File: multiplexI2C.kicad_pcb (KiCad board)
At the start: 2 copper layers, 48.3 x 71.1 mm, 60 parts, among them J1 Screw_Terminal_01x04, J17 Conn_01x04_Pin, J18 PinSocket_1x20_P2.54mm_Vertic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, J19 PinSocket_1x20_P2.54mm_Vertic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, J2 Screw_Terminal_01x04, J20 Screw_Terminal_01x02, J3 Screw_Terminal_01x04, J4 Screw_Terminal_01x04, J5 Screw_Terminal_01x04, J6 Screw_Terminal_01x04, J7 Screw_Terminal_01x04, J8 Screw_Terminal_01x04, J9 header_0.25sqmm_1x04_P4.2mm_D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, U1 TCA9548A, U2 RFM95W-915S2

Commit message: cleaning up details forbetter BOM generator.
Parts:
- J9: value header_0.25sqmm_1x04_P4.2mm_D0.65mm_OD1.7mm -> PinSocket__1x04_P2.54mm_Vertical
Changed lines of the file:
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@@
 		(sheetname "Root")
 		(sheetfile "multiplexI2C.kicad_sch")
-		(attr exclude_from_pos_files)
+		(attr exclude_from_pos_files exclude_from_bom)
 		(fp_circle
 			(center 0 0)
@@
 			)
 		)
-		(property "Description" "Generic screw terminal, single row, 01x04, script generated (kicad-library-utils/schlib/autogen/connector/)"
+		(property "Description" "Generic screw terminal, single row, 01x04"
 			(at 0 0 180)
 			(unlocked yes)
@@
 			)
 		)
-		(property "Description" "Generic screw terminal, single row, 01x04, script generated (kicad-library-utils/schlib/autogen/connector/)"
+		(property "Description" "Generic screw terminal, single row, 01x04"
 			(at 0 0 180)
 			(unlocked yes)
@@
 			)
 		)
-		(property "Description" "Generic screw terminal, single row, 01x04, script generated (kicad-library-utils/schlib/autogen/connector/)"
+		(property "Description" "Generic screw terminal, single row, 01x04"
 			(at 0 0 180)
 			(unlocked yes)
@@
 		(layer "F.Cu")
 		(at 89.916 64.77)
-		(descr "sockets for blackpill stm32f401")
+		(descr "take-off from blackpill stm32f401")
 		(tags "blackpill bluepill pinSockets")
 		(property "Reference" "J**2"
@@
 			)
 		)
-		(property "Description" "extra pads for one side of blackpill (stm32f401) pins 21-40"
+		(property "Description" "unpopulated connections"
 			(at 0 0 0)
 			(unlocked yes)
@@
 		(sheetname "Root")
 		(sheetfile "multiplexI2C.kicad_sch")
-		(attr through_hole)
+		(attr through_hole exclude_from_bom)
 		(fp_line
 			(start -2.286 -25.146)
@@
 			)
 		)
-		(property "Description" "one side of blackpill (stm32f401) pins 21-40"
+		(property "Description" "20P header (for blackpill)"
 			(at 0 0 0)
 			(unlocked yes)
@@
 			)
 		)
-		(property "Description" "Generic screw terminal, single row, 01x04, script generated (kicad-library-utils/schlib/autogen/connector/)"
+		(property "Description" "Generic screw terminal, single row, 01x04"
 			(at 0 0 180)
 			(unlocked yes)
@@
 		(sheetname "Root")
 		(sheetfile "multiplexI2C.kicad_sch")
-		(attr exclude_from_pos_files)
+		(attr exclude_from_pos_files exclude_from_bom)
 		(fp_circle
 			(center 0 0)
@@
 			)
 		)
-		(property "Description" "Generic screw terminal, single row, 01x04, script generated (kicad-library-utils/schlib/autogen/connector/)"
+		(property "Description" "Generic screw terminal, single row, 01x04"
 			(at 0 0 180)
 			(unlocked yes)
@@
 		(sheetname "Root")
 		(sheetfile "multiplexI2C.kicad_sch")
-		(attr exclude_from_pos_files)
+		(attr exclude_from_pos_files exclude_from_bom)
 		(fp_circle
 			(center 0 0)
@@
 			)
 		)
-		(property "Description" "Generic connector, single row, 01x04, script generated"
+		(property "Description" "Generic connector, single row, 01x04"
 			(at 0 0 -90)
 			(unlocked yes)
@@
 			)
 		)
-		(property "Description" "Generic screw terminal, single row, 01x04, script generated (kicad-library-utils/schlib/autogen/connector/)"
+		(property "Description" "Generic screw terminal, single row, 01x04"
 			(at 0 0 180)
 			(unlocked yes)
@@
 		(layer "F.Cu")
 		(at 86.165 64.605)
-		(descr "sockets for blackpill stm32f401")
+		(descr "take-off  from blackpill stm32f401")
 		(tags "blackpill bluepill pinSockets")
 		(property "Reference" "J**1"
@@
 			)
 		)
-		(property "Description" "extra takeoff pads for one side of blackpill (stm32f401) pins 1-20"
+		(property "Description" "unpopulated connections"
 			(at 0 0 0)
 			(unlocked yes)
@@
 		(sheetname "Root")
 		(sheetfile "multiplexI2C.kicad_sch")
-		(attr through_hole)
+		(attr through_hole exclude_from_bom)
 		(fp_line
 			(start -6.096 -25.146)
@@
 			)
 		)
-		(property "Description" "one side of blackpill (stm32f401) pins 1-20"
+		(property "Description" "20P header (for blackpill)"
 			(at 0 0 0)
 			(unlocked yes)
@@
 			)
 		)
-		(property "Description" "Generic screw terminal, single row, 01x04, script generated (kicad-library-utils/schlib/autogen/connector/)"
+		(property "Description" "Generic screw terminal, single row, 01x04"
 			(at 0 0 180)
 			(unlocked yes)
@@
 		(layer "F.Cu")
 		(at 65.61 92.825 -90)
-		(descr "Through hole straight socket strip, 1x04, 2.54mm pitch, single row (from Kicad 4.0.7), script generated")
+		(descr "header for ssd1306")
 		(tags "Through hole socket strip THT 1x04 2.54mm single row")
 		(property "Reference" "J9"
@@
 			)
 		)
-		(property "Value" "header_0.25sqmm_1x04_P4.2mm_D0.65mm_OD1.7mm"
-			(at 6.705 3.55 180)
+		(property "Value" "PinSocket__1x04_P2.54mm_Vertical"
+			(at 23.655 3.43 -90)
 			(layer "F.Fab")
 			(effects
@@
 			)
 		)
-		(property "Description" "4P I2C header for SSD1306 module"
+		(property "Description" "4P header (I2C for SSD1306 module)"
 			(at 0 0 -90)
 			(unlocked yes)
@@
 			)
 		)
+		(property "Manufacturer" "JILN"
+			(at 0 0 -90)
+			(unlocked yes)
+			(layer "F.Fab")
+			(hide yes)
+			(effects
+				(font
+					(size 1 1)
+					(thickness 0.15)
+				)
+			)
+		)
+		(property "MfgPart" "228050104ANG1SYA01"
+			(at 0 0 -90)
+			(unlocked yes)
+			(layer "F.Fab")
+			(hide yes)
+			(effects
+				(font
+					(size 1 1)
+					(thickness 0.15)
+				)
+			)
+		)
+		(property "MountType" "PTH"
+			(at 0 0 -90)
+			(unlocked yes)
+			(layer "F.Fab")
+			(hide yes)
+			(effects
+				(font
+					(size 1 1)
+					(thickness 0.15)
+				)
+			)
+		)
+		(property "Notes" "or equivalent"
+			(at 0 0 -90)
+			(unlocked yes)
+			(layer "F.Fab")
+			(hide yes)
+			(effects
+				(font
+					(size 1 1)
+					(thickness 0.15)
+				)
+			)
+		)
 		(sheetname "Root")
 		(sheetfile "multiplexI2C.kicad_sch")
@@
 		(sheetname "Root")
 		(sheetfile "multiplexI2C.kicad_sch")
-		(attr exclude_from_pos_files)
+		(attr exclude_from_pos_files exclude_from_bom)
 		(fp_circle
 			(center 0 0)
@@
 			)
 		)
-		(property "Description" "Generic screw terminal, single row, 01x02, script generated (kicad-library-utils/schlib/autogen/connector/)"
+		(property "Description" "Generic screw terminal, single row, 01x02"
 			(at 0 0 180)
 			(unlocked yes)
@@
 			)
 		)
-		(property "Description" "Generic screw terminal, single row, 01x04, script generated (kicad-library-utils/schlib/autogen/connector/)"
+		(property "Description" "Generic screw terminal, single row, 01x04"
 			(at 0 0 180)
 			(unlocked yes)
@@
 		)
 		(property "Value" "915mhz antenna"
-			(at -7.29 3.12 270)
+			(at -7.29 3.12 -90)
 			(layer "B.SilkS")
 			(effects
@@
 			)
 		)
-		(property "Datasheet" ""
+		(property "Datasheet" "https://www.nicerf.com/rf-antenna/915mhz-spring-antenna-sw915-th06.html"
 			(at 0 0 -90)
 			(unlocked yes)

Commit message: as ordered 2024-09 with minor changes for part availability.
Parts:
- U1: value TCA9548A -> PCA9548A
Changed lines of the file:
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@@
 			)
 		)
-		(property "Value" "TCA9548A"
+		(property "Value" "PCA9548A"
 			(at -5.5875 -2.385 90)
 			(layer "F.Fab")
@@
 			)
 		)
-		(property "Datasheet" "http://www.ti.com/lit/ds/symlink/tca9548a.pdf"
+		(property "Datasheet" "https://www.nxp.com/products/interfaces/ic-spi-i3c-interface-devices/ic-logic-multiplexers-switches/eight-channel-ic-bus-switch-with-reset:PCA9548A"
 			(at 0 0 0)
 			(unlocked yes)
@@
 			)
 		)
-		(property "Manufacturer" "TI"
+		(property "Manufacturer" "NXP"
 			(at 0 0 0)
 			(unlocked yes)
@@
 			)
 		)
-		(property "MfgPart" "TCA9548A"
+		(property "MfgPart" "PCA9548APW"
 			(at 0 0 0)
 			(unlocked yes)
@@
 		(sheetname "Root")
 		(sheetfile "multiplexI2C.kicad_sch")
-		(attr through_hole)
+		(attr through_hole dnp)
 		(fp_line
 			(start 1.11 0)

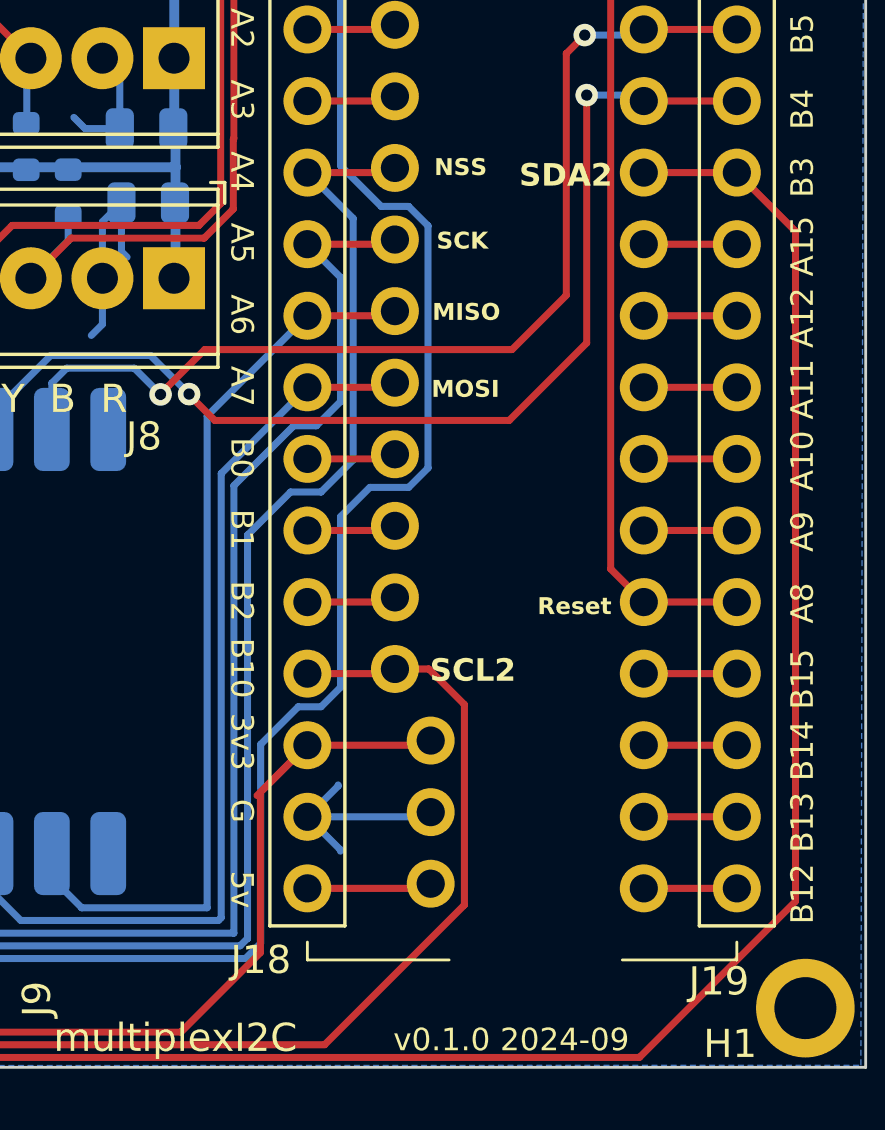
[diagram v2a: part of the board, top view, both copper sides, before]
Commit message: added 10k pullup on NSS.
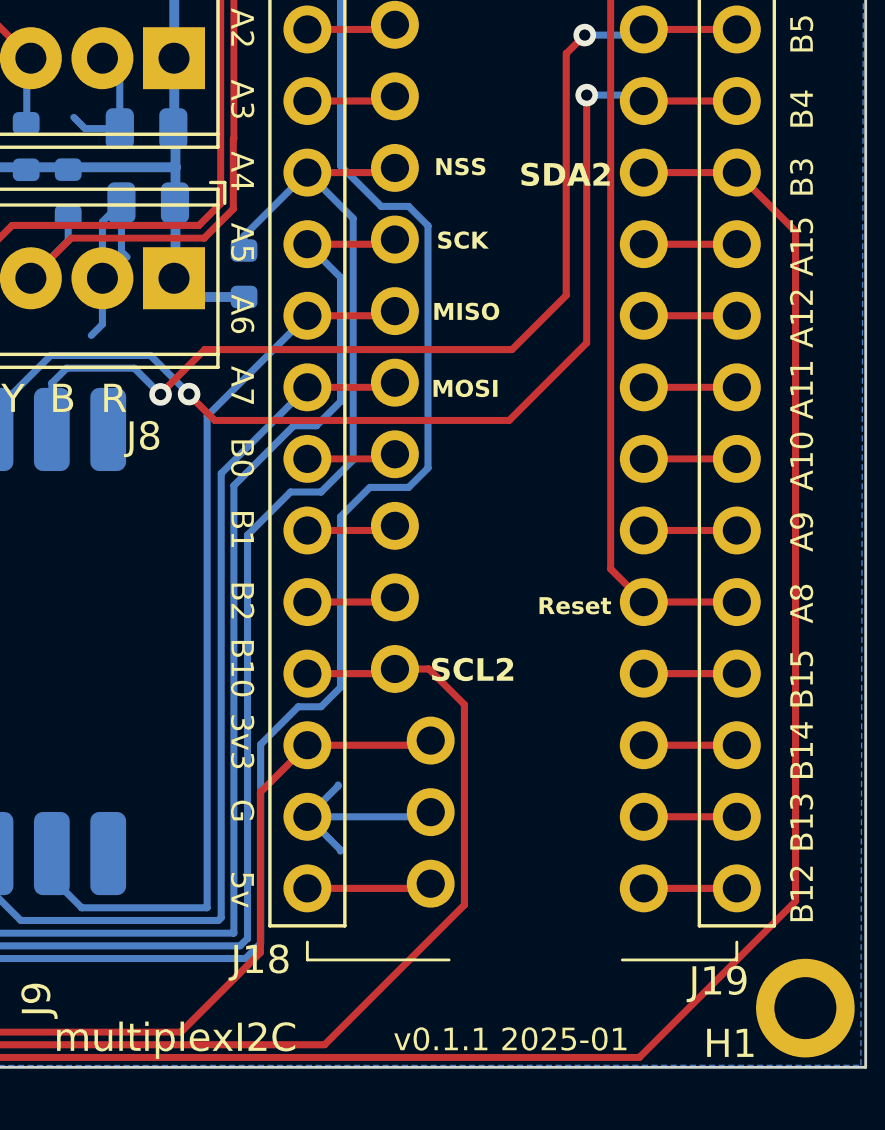
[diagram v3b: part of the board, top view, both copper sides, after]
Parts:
- added R26: 10k, ProjectLib:R_0603_1608Metric, B.Cu at (75.7, 67.1)
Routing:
- net NSS: track 48.4 -> 52.1 mm
- net +3V3: track 174.4 -> 177.1 mm
- net Net-(J18-3v3): track 29.7 -> 27.2 mm
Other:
- board text added: "v0.1.1 2025-01"
- board text removed: "v0.1.0 2024-09"

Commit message: ongoing
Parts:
- removed J**1: SolderWire-0.25sqmm_1x20_P4.2mm_D0.65mm_OD1.7mm, ProjectLib:b_pill_takeoffPads_1-20
- removed J**2: SolderWire-0.25sqmm_1x20_P4.2mm_D0.65mm_OD1.7mm, ProjectLib:b_pill_takeoffPads_21-40
- removed J17: Conn_01x04_Pin, ProjectLib:JST_XH_B4B-XH-A_1x04_P2.50mm_Vertical
- removed J19: PinSocket_1x20_P2.54mm_Vertical, ProjectLib:b_pill_socket_21-40
- removed J9: PinSocket__1x04_P2.54mm_Vertical, ProjectLib:PinSocket_1x04_P2.54mm_Vertical
- added BT1: Battery_Cell_Holder, ProjectLib:BatteryHolder_LINX_BAT-HLD-012-SMT, B.Cu at (87.9, 35.5)
- added C1: 0.1µF, ProjectLib:C_0402_1005Metric, F.Cu at (0.94, 0.48)
- added C10: 10pF C0G, NP0, +/- 0.1pF, ProjectLib:C_0402_1005Metric, F.Cu at (79.1, 46.4)
- added C11: 10pF C0G, NP0, +/- 0.1pF, ProjectLib:C_0402_1005Metric, F.Cu at (81.4, 46.8)
- added C12: 4pF C0G, NP0, +/- 0.1pF, ProjectLib:C_0402_1005Metric, F.Cu at (87.6, 45.5)
- added C13: 4pF C0G, NP0, +/- 0.1pF, ProjectLib:C_0402_1005Metric, F.Cu at (86.9, 44.8)
- added C14: 4.7µF, ProjectLib:C_0402_1005Metric, F.Cu at (81.1, 61.7)
- added C15: 100nF, ProjectLib:C_0402_1005Metric, F.Cu at (78.9, 31.2)
- added C16: 100nF, ProjectLib:C_0402_1005Metric, F.Cu at (91.6, 40.3)
- added C17: 100nF, ProjectLib:C_0402_1005Metric, F.Cu at (75.9, 52.4)
- added C2: 0.1µF, ProjectLib:C_0402_1005Metric, F.Cu at (70.9, 28.0)
- added C22: 0.1µF, ProjectLib:C_0402_1005Metric, F.Cu at (59.9, 28.0)
- added C3: 0.1µF, ProjectLib:C_0402_1005Metric, F.Cu at (62.1, 45.4)
- added C4: 0.1µF, ProjectLib:C_0402_1005Metric, F.Cu at (75.9, 89.1)
- added C9: 100nF, ProjectLib:C_0402_1005Metric, F.Cu at (76.8, 43.0)
- added D1: red 2ma 1.8Vf, ProjectLib:LED_0603_1608Metric, F.Cu at (94.2, 41.6)
- added D2: blue 2ma 2.65Vf, ProjectLib:LED_0603_1608Metric, F.Cu at (91.8, 42.4)
- added D3: BAT54C-HF, Package_TO_SOT_SMD:SOT-23, F.Cu at (88.2, 39.2)
- added L1: 2.2uH, ProjectLib:L_0402_1005Metric, F.Cu at (76.0, 55.2)
- added NT1: NetTie_2, ProjectLib:NetTie-2_SMD_Pad0.5mm, B.Cu at (79.6, 51.4)
- added NT2: NetTie_2, ProjectLib:NetTie-2_SMD_Pad0.5mm, B.Cu at (85.7, 48.7)
- added R17: 4.7k, ProjectLib:R_0402_1005Metric, F.Cu at (76.8, 38.1)
- added R18: 4.7k, ProjectLib:R_0402_1005Metric, F.Cu at (76.8, 36.6)
- added R19: 4.7k, ProjectLib:R_0402_1005Metric, F.Cu at (72.8, 36.5)
- added R23: 715 1%, ProjectLib:R_0402_1005Metric, F.Cu at (93.7, 44.2)
- added R24: 280 1%, ProjectLib:R_0402_1005Metric, F.Cu at (92.6, 44.2)
- added R25: 10k 1%, ProjectLib:R_0402_1005Metric, F.Cu at (91.2, 50.7)
- added R26: 10k 1%, ProjectLib:R_0402_1005Metric, F.Cu at (79.8, 43.1)
- added R27: 10k 1%, ProjectLib:R_0402_1005Metric, F.Cu at (80.1, 61.8)
- added R28: 10k 1%, ProjectLib:R_0402_1005Metric, F.Cu at (78.4, 56.4)
- added R29: 0, ProjectLib:R_0402_1005Metric, F.Cu at (84.8, 44.9)
- added R30: 634 1%, ProjectLib:R_0402_1005Metric, F.Cu at (78.5, 49.3)
- added R31: 10k 1%, ProjectLib:R_0402_1005Metric, F.Cu at (74.5, 55.2)
- added R32: 10k, ProjectLib:R_0402_1005Metric, F.Cu at (54.5, 45.2)
- added R33: 10k 1%, ProjectLib:R_0402_1005Metric, F.Cu at (86.8, 72.6)
- added R34: 10k 1%, ProjectLib:R_0402_1005Metric, F.Cu at (89.6, 72.6)
- added R35: 10k 1%, ProjectLib:R_0402_1005Metric, F.Cu at (72.2, 79.5)
- added SW1: SW_Push, ProjectLib:SW_SPST_B3U-1000P, F.Cu at (77.7, 40.6)
- added SW2: SW_Push, ProjectLib:SW_SPST_B3U-1000P, F.Cu at (83.4, 40.6)
- added TP1: BT1 b2, ProjectLib:TestPoint_Pad_D1.0mm, F.Cu at (80.5, 59.0)
- added TP2: TestPoint_Probe, ProjectLib:TestPoint_Pad_D1.0mm, F.Cu at (80.5, 63.9)
- added U5: STM32F411CEU6, Package_DFN_QFN:QFN-48-1EP_7x7mm_P0.5mm_EP5.6x5.6mm, F.Cu at (84.4, 54.5)
- added U6: AMS1117-3.3 SOT-223, Package_TO_SOT_SMD:SOT-223-3_TabPin2, F.Cu at (86.7, 30.0)
- added Y1: 25MHz, ProjectLib:Crystal_SMD_2016-4Pin_2.0x1.6mm, F.Cu at (80.0, 48.0)
- added Y2: 32.758kHz, ProjectLib:Crystal_SMD_MicroCrystal_CM9V-T1A-2Pin_1.6x1.0mm, F.Cu at (85.8, 46.3)
- AE1: value 915mhz antenna -> U.FL; footprint ProjectLib:915MHz_spring_antenna -> ProjectLib:U.FL_Molex_MCRF_73412-0110_Vertical; moved to F.Cu
- C14: value 0.1µF -> 4.7µF; footprint ProjectLib:C_0805_2012Metric -> ProjectLib:C_0402_1005Metric
- C15, C16, C17, C9: value 0.1µF -> 100nF; footprint ProjectLib:C_0805_2012Metric -> ProjectLib:C_0402_1005Metric
- C18, C19, C20, C21: footprint ProjectLib:C_0805_2012Metric -> ProjectLib:C_0402_1005Metric
- C5: value 10µF -> 1µF; footprint ProjectLib:C_0805_2012Metric -> ProjectLib:C_0402_1005Metric
- C6, C7, C8: value 10µF -> 100nF; footprint ProjectLib:C_0805_2012Metric -> ProjectLib:C_0402_1005Metric
- J18: value PinSocket_1x20_P2.54mm_Vertical -> Conn_02x04_Top_Bottom; footprint ProjectLib:b_pill_socket_1-20 -> ProjectLib:PinSocket_2x04_P2.54mm_Vertical_SMD
- R1, R2, R3: value 10k -> 0; footprint ProjectLib:R_0603_1608Metric -> ProjectLib:R_0402_1005Metric
- R10, R11, R12, R13, R14, R15, R16, R17, R18, R19, R20, R21, R22, R4, R5, R6, R7, R8, R9: footprint ProjectLib:R_0603_1608Metric -> ProjectLib:R_0402_1005Metric
- R23: value 0 -> 715 1%; footprint ProjectLib:R_0603_1608Metric -> ProjectLib:R_0402_1005Metric
- R24: value 0 -> 280 1%; footprint ProjectLib:R_0603_1608Metric -> ProjectLib:R_0402_1005Metric
- R25: value 0 -> 10k 1%; footprint ProjectLib:R_0603_1608Metric -> ProjectLib:R_0402_1005Metric
- R26: value 10k -> 10k 1%; footprint ProjectLib:R_0603_1608Metric -> ProjectLib:R_0402_1005Metric
- U1: footprint ProjectLib:TSSOP-24_4.4x7.8mm_P0.65mm -> Package_SO:TSSOP-24_4.4x7.8mm_P0.65mm
- U2: moved to F.Cu
- moved AE1 44.2 mm to (91.1, 92.6), turned to 180 degrees
- moved U2 22.7 mm to (86.6, 81.8), turned to 0 degrees
- moved J18 11.1 mm to (89.0, 66.5)
- moved C15 5.39 mm to (77.5, 34.3)
- moved J20 2.81 mm to (79.8, 30.0)
- moved C8 2.50 mm to (79.1, 37.3)
- moved C7 2.13 mm to (80.6, 37.3)
- moved C6 1.89 mm to (82.1, 37.3)
- moved C5 1.75 mm to (83.5, 37.3)
- moved J2 1.11 mm to (72.3, 33.3)
- moved J4 1.07 mm to (72.3, 40.9)
- moved J6 1.05 mm to (72.4, 60.0)
- moved J8 1.04 mm to (72.4, 67.8)
- moved R23 0.80 mm to (66.3, 51.6)
- moved C21 0.80 mm to (71.9, 65.2)
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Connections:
- net ANT renamed Net-(AE1-A)
- C14 pad 1: +3V3 -> Net-(U5-VCAP1)
- C15 pad 1: +3V3 -> +5V
- C16 pad 1: +3V3 -> VBAT
- C17 pad 1: +3V3 -> Net-(U5-VDDA/VREF+)
- C9 pad 1: +3V3 -> GND
- C9 pad 2: GND -> Net-(U5-NRST)
- J20 pad 2: +3V3 -> +5V
- R1 pad 1: +3V3 -> Net-(U1-A0)
- R1 pad 2: /SCL1 -> GND
- R2 pad 1: +3V3 -> Net-(U1-A1)
- R2 pad 2: /SDA1 -> GND
- R23 pad 1: Net-(U1-A1) -> Net-(D1-K)
- R24 pad 2: Net-(U1-A2) -> Net-(D2-A)
- R25 pad 1: Net-(U1-A2) -> Net-(U5-BOOT0)
- R26 pad 2: NSS -> Net-(U5-NRST)
- R3 pad 1: +3V3 -> Net-(U1-A2)
- R3 pad 2: Net-(J19-A8) -> GND
- R4 pad 1: Net-(U1-A0) -> +3V3
- R4 pad 2: GND -> Net-(U1-A0)
- R5 pad 2: Net-(U1-A0) -> Net-(U1-A1)
- R6 pad 2: Net-(U1-A1) -> Net-(U1-A2)
- U1 pad 22: /SCL1 -> SCL2
- U1 pad 23: /SDA1 -> SDA2
- U1 pad 3: Net-(J19-A8) -> PA9
- U2 pad 10: GND -> GND_ANT
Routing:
- net +3V3: track 177.1 -> 300.3 mm, vias 4 -> 9
- net /SDA1: track 72.7 -> 0.00 mm
- net /SCL1: track 72.4 -> 0.00 mm
- net /SDA2: track 69.7 -> 0.00 mm
- net Net-(J19-A8): track 67.4 -> 0.00 mm, vias 2 -> 0
- net SDA1: track 0.00 -> 41.9 mm, vias 0 -> 2
- net /SCL2: track 39.0 -> 0.00 mm
- net SCL1: track 0.00 -> 36.9 mm, vias 0 -> 2
- net (no net): track 0.00 -> 31.2 mm, vias 0 -> 2
- net RESET: track 64.7 -> 36.6 mm
- net Net-(J18-3v3): track 27.2 -> 0.00 mm
- net GND_HSE: track 0.00 -> 23.4 mm, vias 0 -> 4
- net /Connector7/SC: track 40.1 -> 17.7 mm
- net NSS: track 52.1 -> 31.1 mm
- net VBAT: track 0.00 -> 20.9 mm
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- added copper zone on B.Cu, net GND_HSE
- added copper zone on B.Cu, net GND_LSE
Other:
- board text added: "-"
- board text added: "."
- board text added: "915MHz"
- board text added: "ADS1115IDGS"
- board text added: "BT0"
- board text added: "BT1"
- board text added: "Battery_Cell_Holder"
- board text added: "CR1216 3v"
- board text added: "H1"
- board text added: "RST"
- board text added: "SLC1"
- board text added: "SWCLK"
- board text added: "SWDI0"
- board text added: "U1"
- board text added: "U2"
- board text added: "a8"
- board text added: "b2 BT1"
- board text added: "b8"
- board text added: "b9"
- board text added: "th8-F411"
- board text added: "v0.2.0 2025-09"
- board text removed: "MISO"
- board text removed: "MOSI"
- board text removed: "NSS"
- board text removed: "Reset"
- board text removed: "SCK"
- board text removed: "SCL1"
- board text removed: "SCL2"
- board text removed: "SDA2"
- board text removed: "SPI Reset"
- board text removed: "VCC"
- board text removed: "multiplexI2C"
- board text removed: "v0.1.1 2025-01"
